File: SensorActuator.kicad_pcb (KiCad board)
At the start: 2 copper layers, 50 x 50 mm, 46 parts, among them IC1 STM32L051K8T6, P1 CONN_02X06, P3 CONN_02X04, P4 CONN_01X04, P5 CONN_01X02, Q1 PMosfetGen, Q2 PMosfetGen, Q4 PMosfetGen, Q5 AO3401, SW1 SW_PUSH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

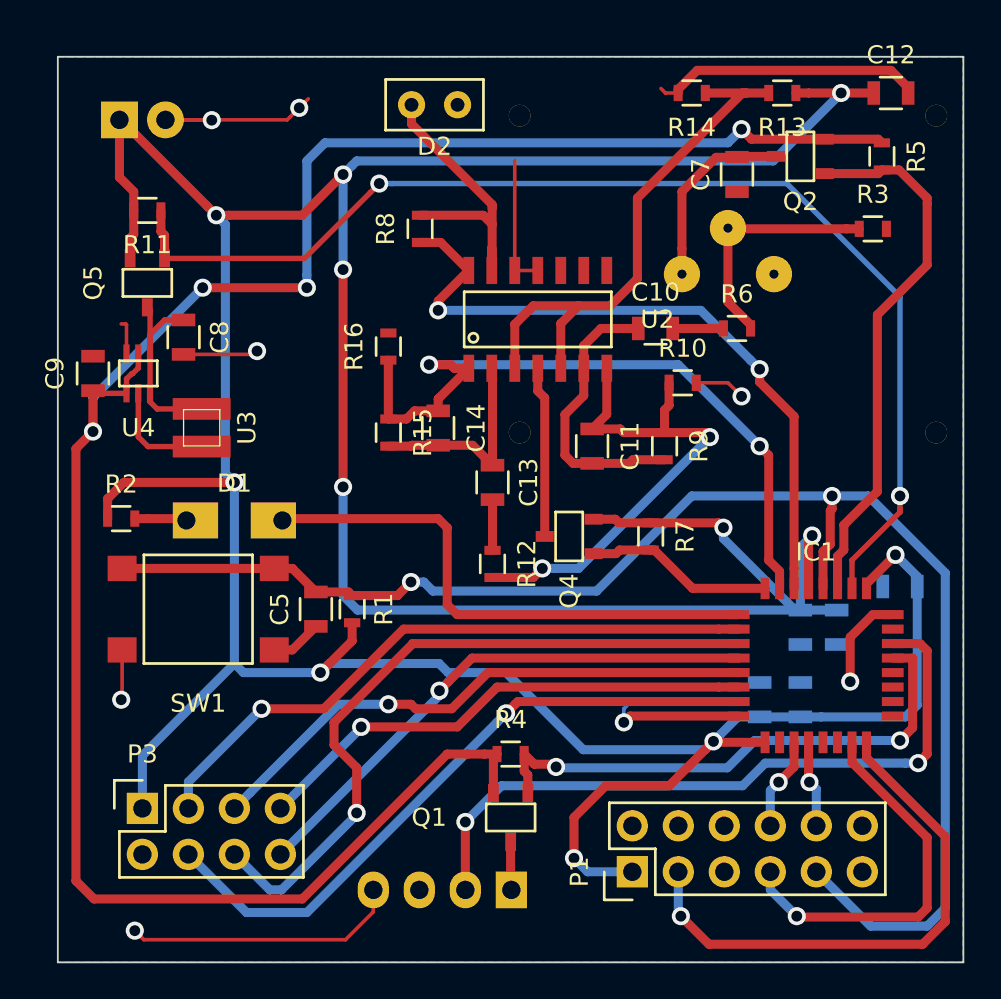
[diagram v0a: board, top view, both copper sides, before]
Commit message: Update pull-up resistor for a sensor
Signed-off-by: Philip Luyckx <philip.luyckx@gmail.com>
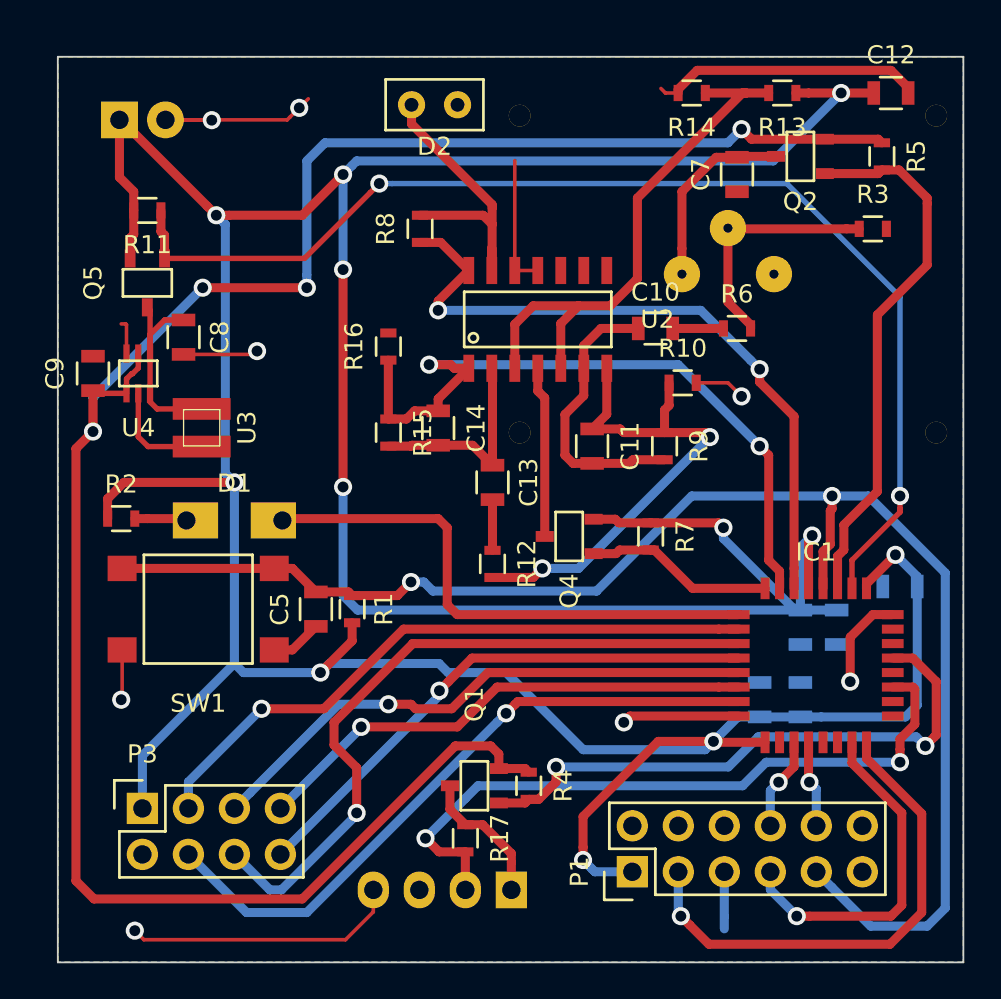
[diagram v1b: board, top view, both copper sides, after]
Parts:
- added R17: 1k, Resistors_SMD:R_0603, F.Cu at (140.5, 111.9)
- moved Q1 2.66 mm to (141.0, 109.0), turned to 90 degrees
- moved R4 2.02 mm to (144.0, 109.0), turned to 270 degrees
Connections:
- IC1 pad 27: (no net) -> Temp_1Wire
- IC1 pad 30: Temp_1Wire -> (no net)
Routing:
- net Net-(P4-Pad1): track 2.67 -> 7.77 mm
- net DHT22_Enable: track 29.9 -> 32.5 mm
- net SWDCLK: track 30.0 -> 27.8 mm
- net SWDIO: track 21.4 -> 19.2 mm
- net GND: track 76.6 -> 78.3 mm
- net +BATT: track 247.2 -> 246.3 mm
- net +5V: track 117.4 -> 118.1 mm

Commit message: Finish work on V2
 * Rework layout
 * Reassign mcu pins
 * Add a capacitor for the RF module

Signed-off-by: Philip Luyckx <philip.luyckx@gmail.com>
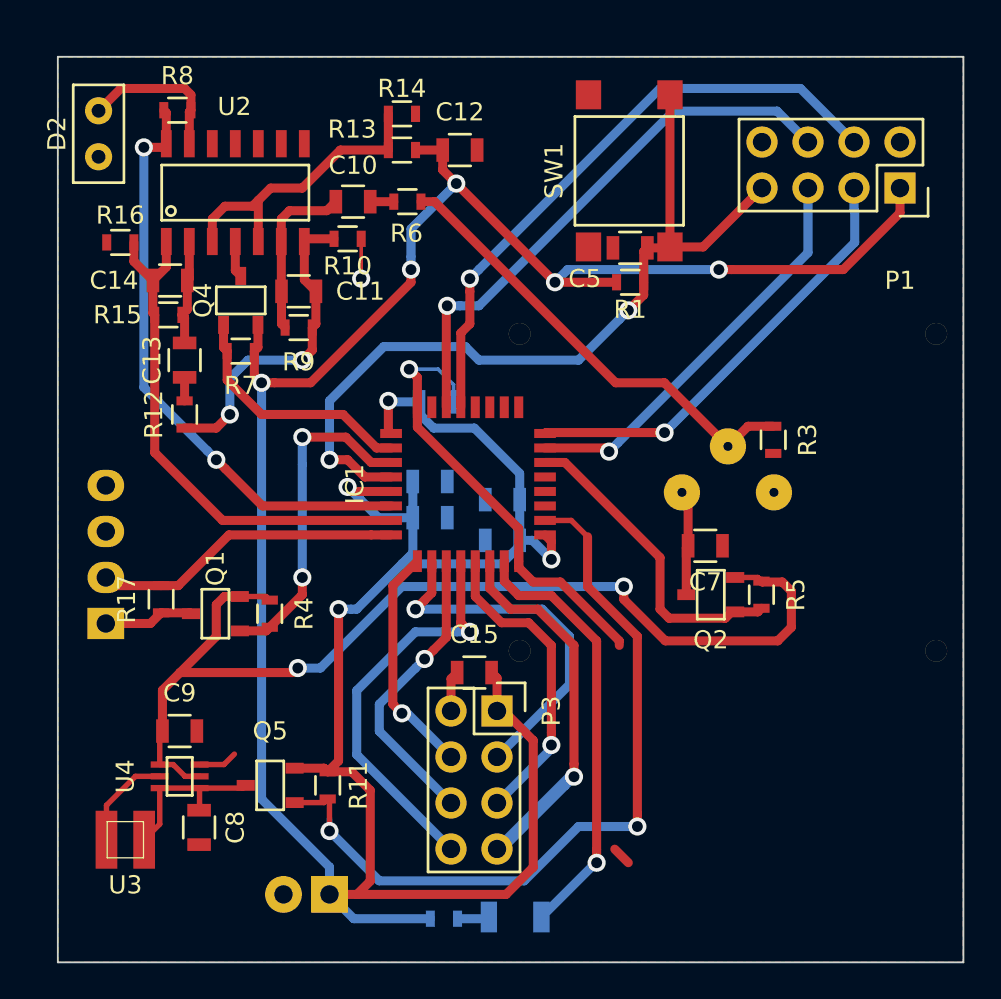
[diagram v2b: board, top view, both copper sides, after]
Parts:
- added C15: C, Resistors_SMD:R_0805, F.Cu at (141.0, 102.8)
- D1: footprint CustomSmd:R_ThroughHole_SMD1206 -> Resistors_SMD:R_1206; moved to B.Cu
- P1: value CONN_02X06 -> CONN_02X04; footprint Pin_Headers:Pin_Header_Straight_2x06 -> Socket_Strips:Socket_Strip_Straight_2x04
- R2: moved to B.Cu
- moved P5 44.3 mm to (133.0, 115.0), turned to 180 degrees
- moved P1 40.5 mm to (164.5, 76.0), turned to 180 degrees
- moved SW1 33.9 mm to (149.6, 75.0), turned to 270 degrees
- moved R11 33.3 mm to (132.9, 109.0), turned to 90 degrees
- moved Q5 28.6 mm to (129.7, 109.0), turned to 90 degrees
- moved R2 28.4 mm to (139.3, 116.3)
- moved C6 27.6 mm to (138.9, 87.8), turned to 0 degrees
- moved C8 27.1 mm to (125.8, 111.3)
- moved P4 26.8 mm to (120.7, 100.0), turned to 90 degrees
- moved C5 26.4 mm to (149.6, 79.3), turned to 180 degrees
- moved D1 25.5 mm to (143.2, 116.2)
- moved R5 25.1 mm to (156.8, 98.5)
- moved R7 24.8 mm to (128.1, 85.0), turned to 180 degrees
- moved Q2 24.7 mm to (154.1, 98.5)
- moved C12 24.0 mm to (140.2, 73.9)
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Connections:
- IC1 pad 15: RF_CE -> MCU_LED
- IC1 pad 18: (no net) -> Enable5V
- IC1 pad 19: UART_TX -> Net-(IC1-Pad19)
- IC1 pad 2: Enable5V -> OpampEnable
- IC1 pad 20: UART_RX -> Net-(IC1-Pad20)
- IC1 pad 21: (no net) -> Net-(IC1-Pad21)
- IC1 pad 22: (no net) -> MotionSens_Enable
- IC1 pad 25: (no net) -> Net-(IC1-Pad25)
- IC1 pad 26: (no net) -> Net-(IC1-Pad26)
- IC1 pad 27: Temp_1Wire -> Net-(IC1-Pad27)
- IC1 pad 28: (no net) -> Net-(IC1-Pad28)
- IC1 pad 29: DHT22_Enable -> UART_TX
- IC1 pad 3: MotionSens_Enable -> DHT22_Enable
- IC1 pad 30: (no net) -> UART_RX
- IC1 pad 31: (no net) -> Net-(IC1-Pad31)
- IC1 pad 8: LightSensEnable -> Temp_1Wire
- IC1 pad 9: MCU_LED -> RF_CE
- P1 pad 4: (no net) -> UART_TX
- P1 pad 5: GND -> SWDIO
- P1 pad 6: (no net) -> UART_RX
- P1 pad 7: SWDIO -> MCU_RST
- P1 pad 8: UART_TX -> Net-(P1-Pad8)
- Q4 pad 1: LightSensEnable -> OpampEnable
- R7 pad 2: LightSensEnable -> OpampEnable
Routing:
- net +BATT: track 246.3 -> 178.8 mm, vias 12 -> 9
- net +5V: track 118.1 -> 58.9 mm, vias 4 -> 2
- net GND: track 78.3 -> 31.6 mm, vias 8 -> 2
- net MCU_RST: track 83.2 -> 46.2 mm
- net UART_TX: track 5.15 -> 34.1 mm
- net UART_RX: track 4.79 -> 30.7 mm
- net RF_CE: track 36.5 -> 12.9 mm
- net SPI_RF_SCK: track 39.0 -> 16.5 mm
- net Enable5V: track 64.8 -> 43.7 mm
- net Temp_1Wire: track 38.2 -> 17.1 mm, vias 2 -> 0
- net RF_CSN: track 35.3 -> 20.5 mm
- net DHT22_Enable: track 32.5 -> 18.5 mm
- net SPI_RF_MOSI: track 31.2 -> 17.2 mm
- net OpampEnable: track 0.00 -> 13.7 mm
- net Motion_Offset: track 30.5 -> 16.8 mm
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
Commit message: Only use one ground plane and reduce pcb size
Signed-off-by: Philip Luyckx <philip.luyckx@gmail.com>
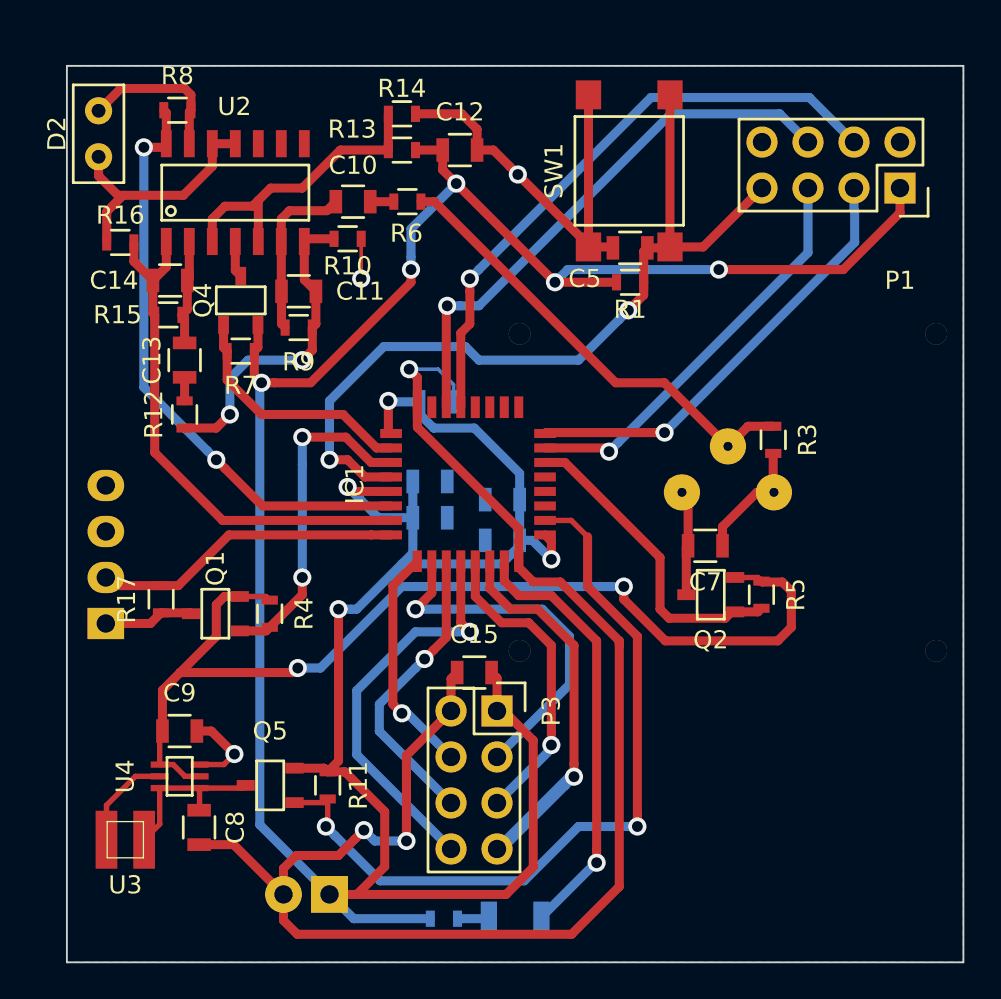
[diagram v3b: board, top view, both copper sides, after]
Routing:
- net GND: track 31.6 -> 136.4 mm, vias 2 -> 6
- net (no net): track 1.06 -> 0.00 mm
- net Enable5V: track 43.7 -> 43.0 mm
- net +BATT: track 178.8 -> 179.4 mm
- removed copper zone on F.Cu, net GND
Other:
- board size 50 x 50 mm -> 49.5 x 49.5 mm
